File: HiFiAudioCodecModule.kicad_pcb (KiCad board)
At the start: 2 copper layers, 25.4 x 25.4 mm, 26 parts, among them P1 CONN_01X06, P2 CONN_01X06, P3 CONN_02X05, U1 AK4558EN

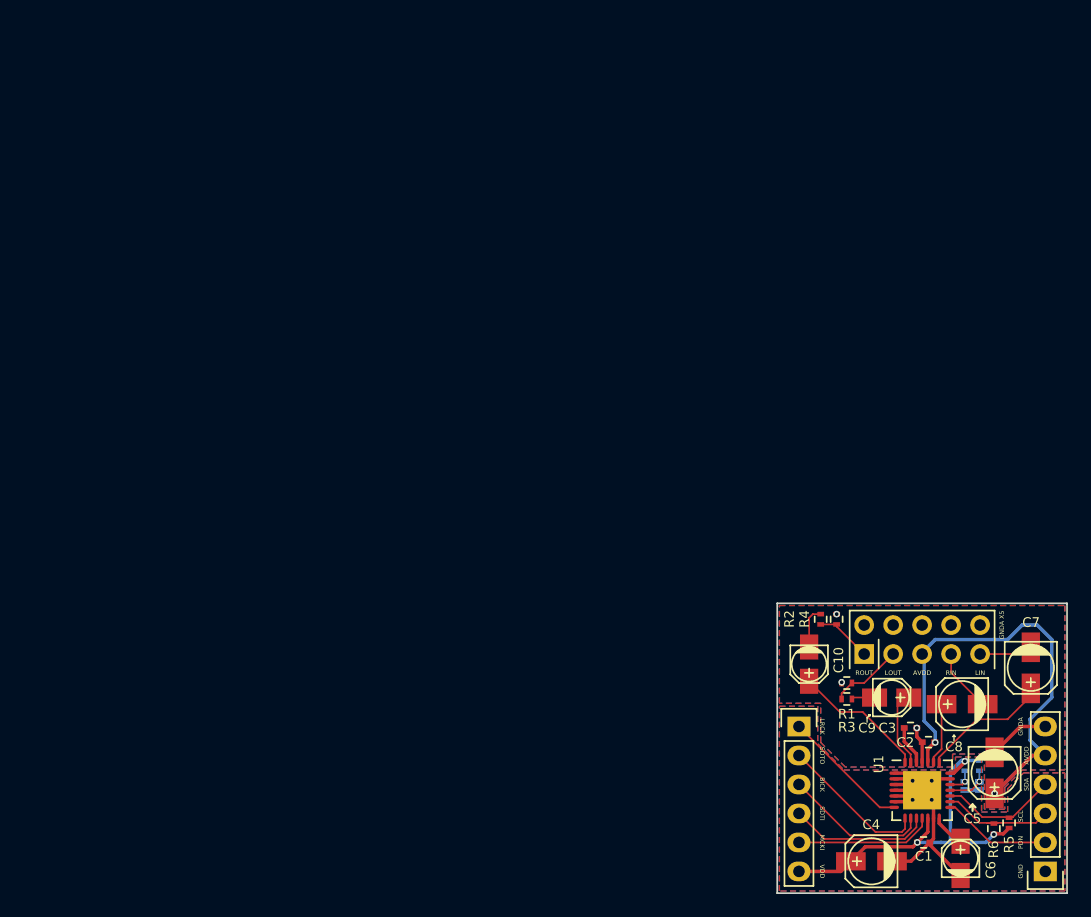
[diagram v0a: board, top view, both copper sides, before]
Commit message: Revised PCB page layout
Revised PCB page layout
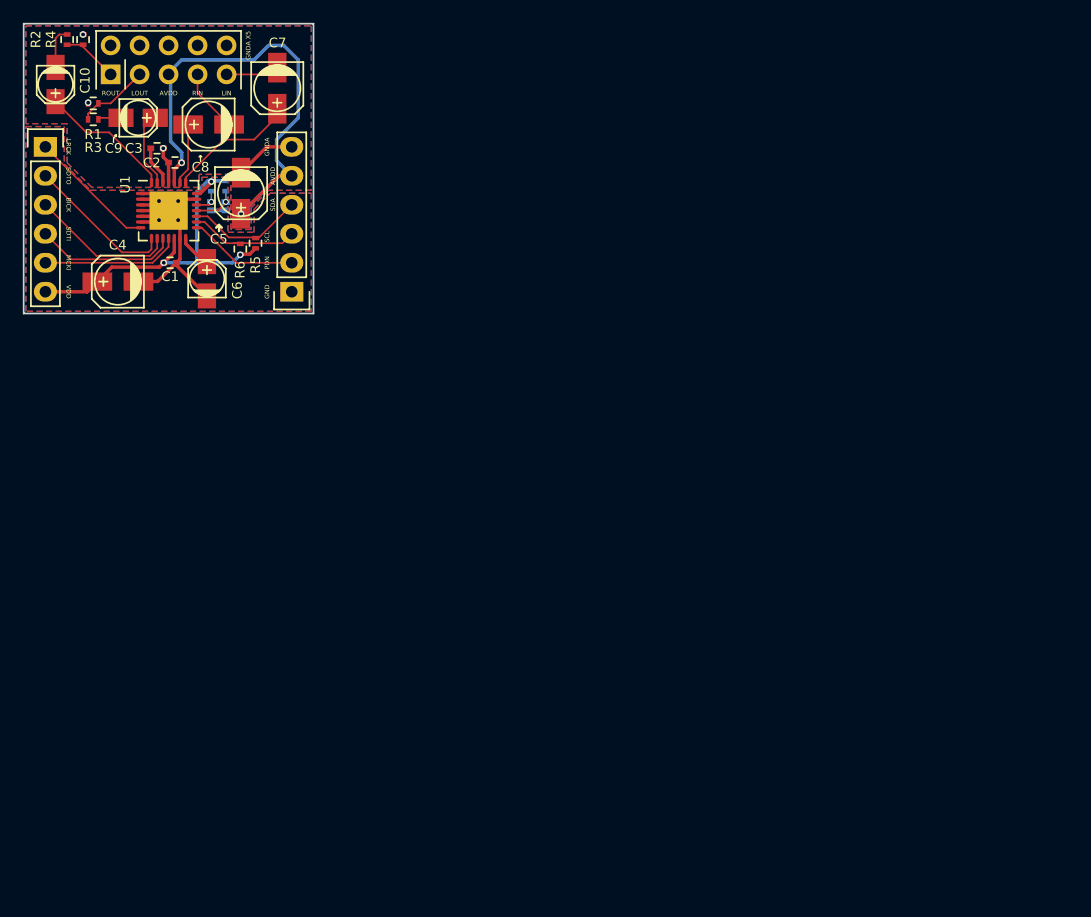
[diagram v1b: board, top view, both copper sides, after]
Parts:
- moved C10 83.3 mm to (15.5, 18.0)
- moved C2 83.3 mm to (26.0, 24.9)
- moved C3 83.3 mm to (24.4, 23.6)
- moved C4 83.3 mm to (21.0, 35.3)
- moved C5 83.3 mm to (31.8, 27.6)
- moved C6 83.3 mm to (28.8, 35.1)
- moved C7 83.3 mm to (34.9, 18.4)
- moved C8 83.3 mm to (28.9, 21.5)
- moved JP1 83.3 mm to (30.4, 28.7)
- moved LOGO1 83.3 mm to (20.3, 34.3)
- moved LOGO2 83.3 mm to (30.5, 34.3)
- moved P2 83.3 mm to (36.2, 36.2)
- moved R1 83.3 mm to (18.8, 21.1)
- moved R2 83.3 mm to (16.5, 14.1)
- moved R4 83.3 mm to (17.9, 14.1)
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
